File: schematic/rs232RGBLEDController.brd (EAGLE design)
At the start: 30 x 35 mm, 41 parts, among them IC1 WS2811-SOP8, J1 AVR_SPI_PRG_62X3_LOCK, Q4 MOSFET-NCHANNELBSS123LT1G, U1 V_REG_LDOSMD, U3 ATMEGA8A-AU-TQFP32, X1 CRYSTALS-NOGND-HC49

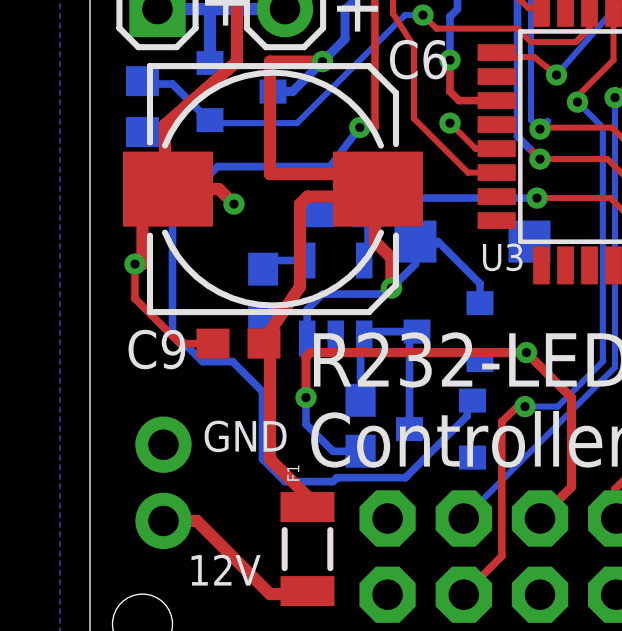
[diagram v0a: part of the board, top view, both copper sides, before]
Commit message: Added additional ground path for the LED.
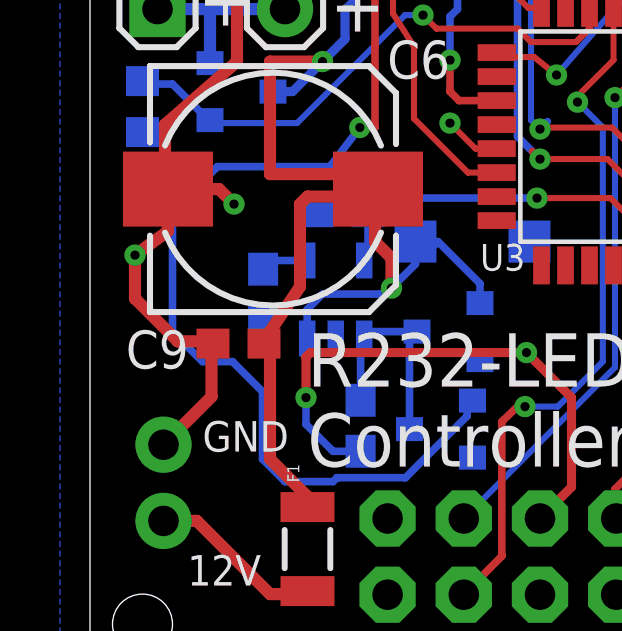
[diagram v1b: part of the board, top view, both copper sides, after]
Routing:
- net GND: track 60.4 -> 64.3 mm
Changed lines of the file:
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@@
 <contactref element="C1" pad="2"/>
 <via x="15.75" y="33.25" extent="1-16" drill="0.3048"/>
-<wire x1="1.75" y1="15.75" x2="2.6" y2="16.25" width="0.4064" layer="1"/>
-<wire x1="1.75" y1="15.75" x2="1.75" y2="13.75" width="0.4064" layer="1"/>
-<wire x1="1.5" y1="13.75" x2="1.75" y2="13.75" width="0.4064" layer="1"/>
-<via x="1.5" y="13.75" extent="1-16" drill="0.3048"/>
+<via x="1.5" y="14.05" extent="1-16" drill="0.3048"/>
 <wire x1="10.2766" y1="28.095" x2="11.595" y2="28.095" width="0.4064" layer="1"/>
 <wire x1="11.595" y1="28.095" x2="12.25" y2="28.75" width="0.4064" layer="1"/>
@@
 <wire x1="17" y1="33.25" x2="17.15" y2="33.4" width="0.254" layer="1"/>
 <wire x1="2.5" y1="18.4" x2="2.5" y2="16.35" width="0.4064" layer="1"/>
-<wire x1="2.5" y1="16.35" x2="2.6" y2="16.25" width="0.4064" layer="1"/>
+<wire x1="2.6" y1="16.25" x2="2.5" y2="16.35" width="0.4064" layer="1"/>
 <wire x1="2.6" y1="16.25" x2="4.3" y2="16.25" width="0.4064" layer="1"/>
 <wire x1="4.3" y1="16.25" x2="4.8" y2="15.75" width="0.4064" layer="1"/>
@@
 <wire x1="7.2" y1="10.65" x2="7.35" y2="10.8" width="0.3048" layer="1"/>
 <contactref element="C9" pad="2"/>
-<wire x1="4.1" y1="11.1" x2="3" y2="11.1" width="0.254" layer="1"/>
-<wire x1="3" y1="11.1" x2="1.5" y2="12.6" width="0.254" layer="1"/>
-<wire x1="1.5" y1="12.6" x2="1.5" y2="13.75" width="0.254" layer="1"/>
 <wire x1="8.1" y1="7.51" x2="9.02" y2="7.51" width="0.254" layer="16"/>
 <wire x1="7.2" y1="9.3" x2="7.2" y2="8.41" width="0.254" layer="16"/>
@@
 <wire x1="12.85" y1="17.6" x2="12" y2="18.45" width="0.2032" layer="1"/>
 <via x="12" y="18.45" extent="1-16" drill="0.3048"/>
+<wire x1="2.45" y1="7.73" x2="4.05" y2="9.33" width="0.4064" layer="1"/>
+<wire x1="4.1" y1="11.1" x2="4.025" y2="11.175" width="0.4064" layer="1"/>
+<wire x1="4.025" y1="11.175" x2="2.925" y2="11.175" width="0.4064" layer="1"/>
+<wire x1="1.5" y1="14.05" x2="2.6" y2="14.85" width="0.4064" layer="1"/>
+<wire x1="2.6" y1="14.85" x2="2.6" y2="16.25" width="0.4064" layer="1"/>
+<wire x1="2.925" y1="11.175" x2="1.5" y2="12.6" width="0.4064" layer="1"/>
+<wire x1="1.5" y1="12.6" x2="1.5" y2="14.05" width="0.4064" layer="1"/>
+<wire x1="4.05" y1="11.05" x2="4.1" y2="11.1" width="0.4064" layer="1"/>
+<wire x1="4.05" y1="9.33" x2="4.05" y2="11.05" width="0.4064" layer="1"/>
 </signal>
 <signal name="TX">
